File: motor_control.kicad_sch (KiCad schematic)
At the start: 4 parts, among them U3 DRV8870DDA

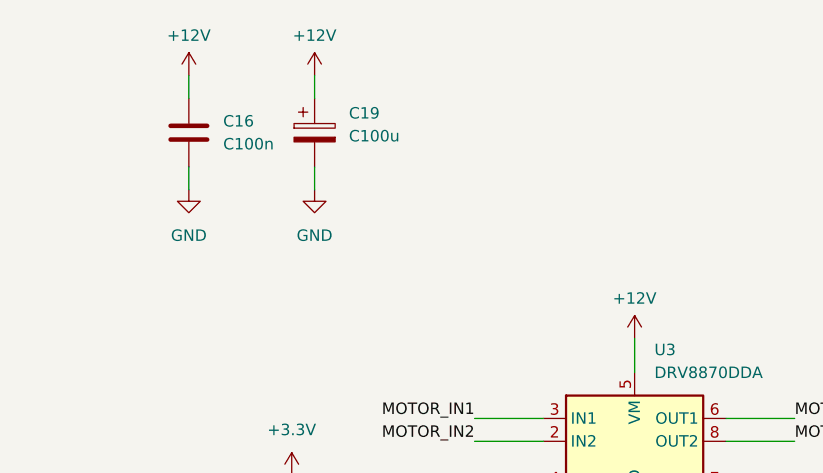
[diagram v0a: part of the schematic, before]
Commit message: Remove 12V buck converter and power rail
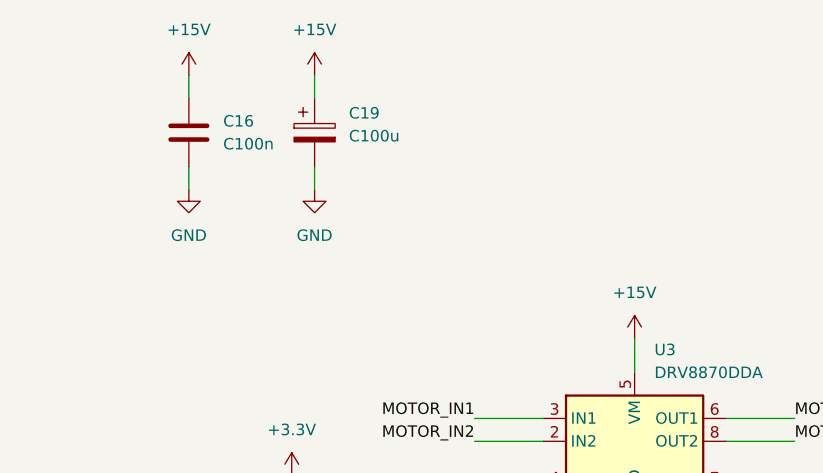
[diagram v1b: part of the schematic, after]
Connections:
- net +12V: no longer C16.1, C19.1, U3.5 (VM)
- new net +15V: C16.1, C19.1, U3.5 (VM)
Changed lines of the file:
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@@
+    )
+  )
+  (symbol (lib_id "power:+15V") (at 156.21 83.82 0) (unit 1)
+    (in_bom yes) (on_board yes) (dnp no) (fields_autoplaced)
+    (property "Reference" "#PWR033" (at 156.21 87.63 0)
+      (effects (font (size 1.27 1.27)) hide)
+    )
+    (property "Value" "+15V" (at 156.21 78.74 0)
+      (effects (font (size 1.27 1.27)))
+    )
+    (property "Footprint" "" (at 156.21 83.82 0)
+      (effects (font (size 1.27 1.27)) hide)
+    )
+    (property "Datasheet" "" (at 156.21 83.82 0)
+      (effects (font (size 1.27 1.27)) hide)
+    )
+    (pin "1")
+    (instances
+      (project "mainboard"
+        (path "/613f8c39-c37c-4981-8911-5138d36a7959/ecb72cc6-9992-49a0-afcf-3c2905614ae7"
+          (reference "#PWR033") (unit 1)
+        )
+      )
+    )
+  )
+  (symbol (lib_id "power:+15V") (at 106.68 54.61 0) (unit 1)
+    (in_bom yes) (on_board yes) (dnp no) (fields_autoplaced)
+    (property "Reference" "#PWR031" (at 106.68 58.42 0)
+      (effects (font (size 1.27 1.27)) hide)
+    )
+    (property "Value" "+15V" (at 106.68 49.53 0)
+      (effects (font (size 1.27 1.27)))
+    )
+    (property "Footprint" "" (at 106.68 54.61 0)
+      (effects (font (size 1.27 1.27)) hide)
+    )
+    (property "Datasheet" "" (at 106.68 54.61 0)
+      (effects (font (size 1.27 1.27)) hide)
+    )
+    (pin "1")
+    (instances
+      (project "mainboard"
+        (path "/613f8c39-c37c-4981-8911-5138d36a7959/ecb72cc6-9992-49a0-afcf-3c2905614ae7"
+          (reference "#PWR031") (unit 1)
+        )
+      )
+    )
+  )
+  (symbol (lib_id "power:+15V") (at 120.65 54.61 0) (unit 1)
+    (in_bom yes) (on_board yes) (dnp no) (fields_autoplaced)
+    (property "Reference" "#PWR032" (at 120.65 58.42 0)
+      (effects (font (size 1.27 1.27)) hide)
+    )
+    (property "Value" "+15V" (at 120.65 49.53 0)
+      (effects (font (size 1.27 1.27)))
+    )
+    (property "Footprint" "" (at 120.65 54.61 0)
+      (effects (font (size 1.27 1.27)) hide)
+    )
+    (property "Datasheet" "" (at 120.65 54.61 0)
+      (effects (font (size 1.27 1.27)) hide)
+    )
+    (pin "1")
+    (instances
+      (project "mainboard"
+        (path "/613f8c39-c37c-4981-8911-5138d36a7959/ecb72cc6-9992-49a0-afcf-3c2905614ae7"
+          (reference "#PWR032") (unit 1)
+        )
+      )
     )
   )
@@
     )
   )
-  (symbol (lib_id "power:+12V") (at 156.21 83.82 0) (unit 1)
-    (in_bom yes) (on_board yes) (dnp no) (fields_autoplaced)
-    (property "Reference" "#PWR045" (at 156.21 87.63 0)
-      (effects (font (size 1.27 1.27)) hide)
-    )
-    (property "Value" "+12V" (at 156.21 79.375 0)
-      (effects (font (size 1.27 1.27)))
-    )
-    (property "Footprint" "" (at 156.21 83.82 0)
-      (effects (font (size 1.27 1.27)) hide)
-    )
-    (property "Datasheet" "" (at 156.21 83.82 0)
-      (effects (font (size 1.27 1.27)) hide)
-    )
-    (pin "1")
-    (instances
-      (project "mainboard"
-        (path "/613f8c39-c37c-4981-8911-5138d36a7959/ecb72cc6-9992-49a0-afcf-3c2905614ae7"
-          (reference "#PWR045") (unit 1)
-        )
-      )
-    )
-  )
-  (symbol (lib_id "power:+12V") (at 120.65 54.61 0) (unit 1)
-    (in_bom yes) (on_board yes) (dnp no) (fields_autoplaced)
-    (property "Reference" "#PWR043" (at 120.65 58.42 0)
-      (effects (font (size 1.27 1.27)) hide)
-    )
-    (property "Value" "+12V" (at 120.65 50.165 0)
-      (effects (font (size 1.27 1.27)))
-    )
-    (property "Footprint" "" (at 120.65 54.61 0)
-      (effects (font (size 1.27 1.27)) hide)
-    )
-    (property "Datasheet" "" (at 120.65 54.61 0)
-      (effects (font (size 1.27 1.27)) hide)
-    )
-    (pin "1")
-    (instances
-      (project "mainboard"
-        (path "/613f8c39-c37c-4981-8911-5138d36a7959/ecb72cc6-9992-49a0-afcf-3c2905614ae7"
-          (reference "#PWR043") (unit 1)
-        )
-      )
-    )
-  )
   (symbol (lib_id "Device:R") (at 173.99 106.68 0) (unit 1)
     (in_bom yes) (on_board yes) (dnp no) (fields_autoplaced)
@@
         )
       )
-    )
-  )
-  (symbol (lib_id "power:+12V") (at 106.68 54.61 0) (unit 1)
-    (in_bom yes) (on_board yes) (dnp no) (fields_autoplaced)
-    (property "Reference" "#PWR040" (at 106.68 58.42 0)
-      (effects (font (size 1.27 1.27)) hide)
-    )
-    (property "Value" "+12V" (at 106.68 50.165 0)
-      (effects (font (size 1.27 1.27)))
-    )
-    (property "Footprint" "" (at 106.68 54.61 0)
-      (effects (font (size 1.27 1.27)) hide)
-    )
-    (property "Datasheet" "" (at 106.68 54.61 0)
-      (effects (font (size 1.27 1.27)) hide)
-    )
-    (pin "1")
-    (instances
-      (project "mainboard"
-        (path "/613f8c39-c37c-4981-8911-5138d36a7959/ecb72cc6-9992-49a0-afcf-3c2905614ae7"
-          (reference "#PWR040") (unit 1)
-        )
-      )
